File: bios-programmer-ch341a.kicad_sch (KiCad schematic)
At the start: 32 parts, among them J1 USB_B_Micro, J10 Conn_02x04_Counter_Clockwise, J2 SPI Debug, J3 I²C Debug, J4 +Banana+, J5 -Banana-, J6 Conn_02x04_Counter_Clockwise, J7 Conn_02x04_Counter_Clockwise, J8 ZIF16, J9 Conn_02x04_Counter_Clockwise, SW1 RESET, U1 CH341A, U2 ISO6741, U3 ADUM1252, Y1 12M

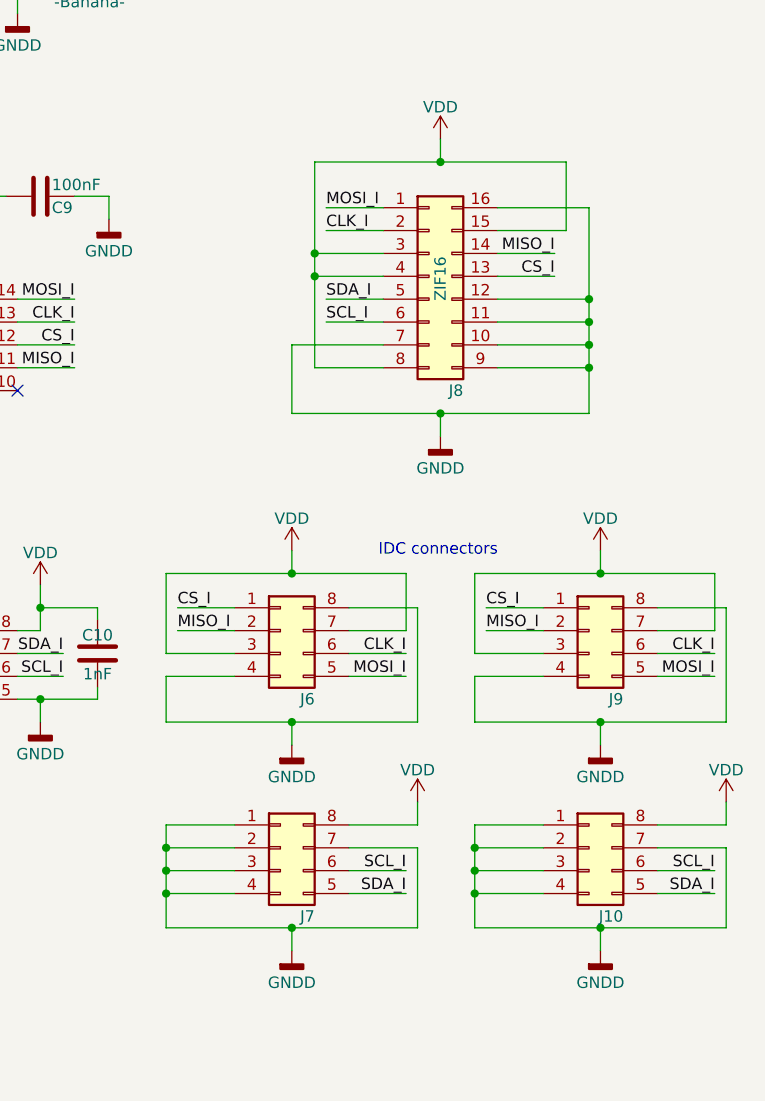
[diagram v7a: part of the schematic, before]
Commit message: PCB: Fixed the ZIF socket layout, pin 1 is pin 1 on SPI (NOT EEPROM)
I still keep the 25/24 order simply because the layout gets much worse if I
change these up. There will be a very clear silkscreen explaining which chip
goes in which part of the socket (including the pinout).

PROBLEM: I did notice that one the left side of the PCB there's GND and GNDD
overlapping each other. Unless I can fix this easily another way, I can only
see one possible fix: place U3 (I2C isolator) in-between the J8 (IDC connector)
and U1 (the CH341 IC).
Most likely this will mean there is no more room to place the debug headers,
permanently or temporarily.
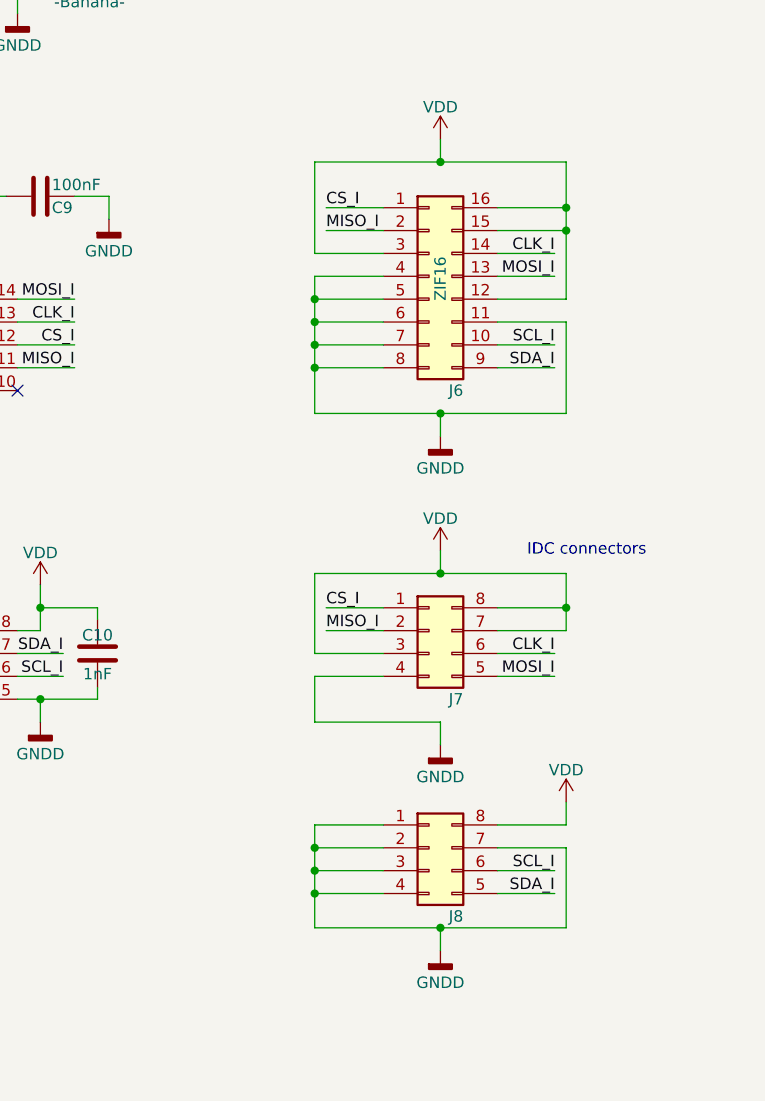
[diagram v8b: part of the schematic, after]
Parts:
- removed J10, J9: Conn_02x04_Counter_Clockwise, Connector_IDC:IDC-Header_2x04_P2.54mm_Horizontal, symbol Connector_Generic:Conn_02x04_Counter_Clockwise
- renumbered J8 to J6, J6 to J7, J7 to J8
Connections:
- net CLK_I: now also J6.14 (Pin_14); no longer J6.2 (Pin_2)
- net CS_I: now also J6.1 (Pin_1); no longer J6.13 (Pin_13)
- net GNDD: now also J6.4 (Pin_4), J6.5 (Pin_5), J6.6 (Pin_6), J6.8 (Pin_8); no longer J6.10 (Pin_10), J6.12 (Pin_12), J6.16 (Pin_16), J6.9 (Pin_9), J7.8 (Pin_8)
- net MISO_I: now also J6.2 (Pin_2); no longer J6.14 (Pin_14)
- net MOSI_I: now also J6.13 (Pin_13); no longer J6.1 (Pin_1)
- net SCL_I: now also J6.10 (Pin_10); no longer J6.6 (Pin_6)
- net SDA_I: now also J6.9 (Pin_9); no longer J6.5 (Pin_5)
- net VDD: now also J6.12 (Pin_12), J6.16 (Pin_16), J7.8 (Pin_8); no longer J6.4 (Pin_4), J6.8 (Pin_8)
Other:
- moved on the sheet: J7, J8
